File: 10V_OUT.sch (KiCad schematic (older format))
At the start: 25 parts, among them U8 LM324

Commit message: Finished the schematic, except for maybe a couple test points.
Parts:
- removed U8: LM324, Package_DIP:DIP-14_W7.62mm, symbol Amplifier_Operational:LM324
- added U10: TLV9304IDR, Package_SO:SOIC-14_3.9x8.7mm_P1.27mm, symbol Amplifier_Operational:TLV9004xRUCR
- renumbered C27 to C36, C28 to C37, C29 to C38, C30 to C39, C31 to C40, C32 to C41, C33 to C42, C34 to C43, R62 to R65, R63 to R66, R64 to R67, R65 to R68, R66 to R69, R67 to R70, R68 to R71, R69 to R72, R70 to R73, R71 to R74, R72 to R75, R73 to R76, R74 to R77, R75 to R78, R76 to R79, R77 to R80

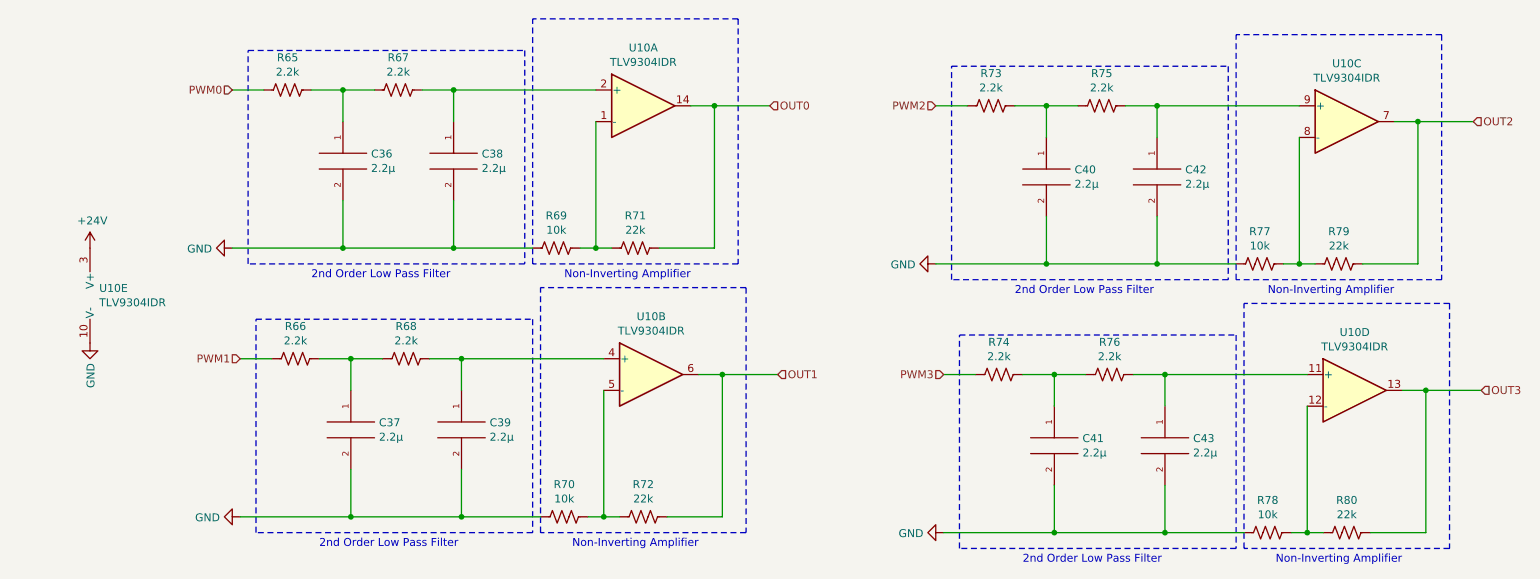
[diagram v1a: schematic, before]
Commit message: Routing for all analog outputs
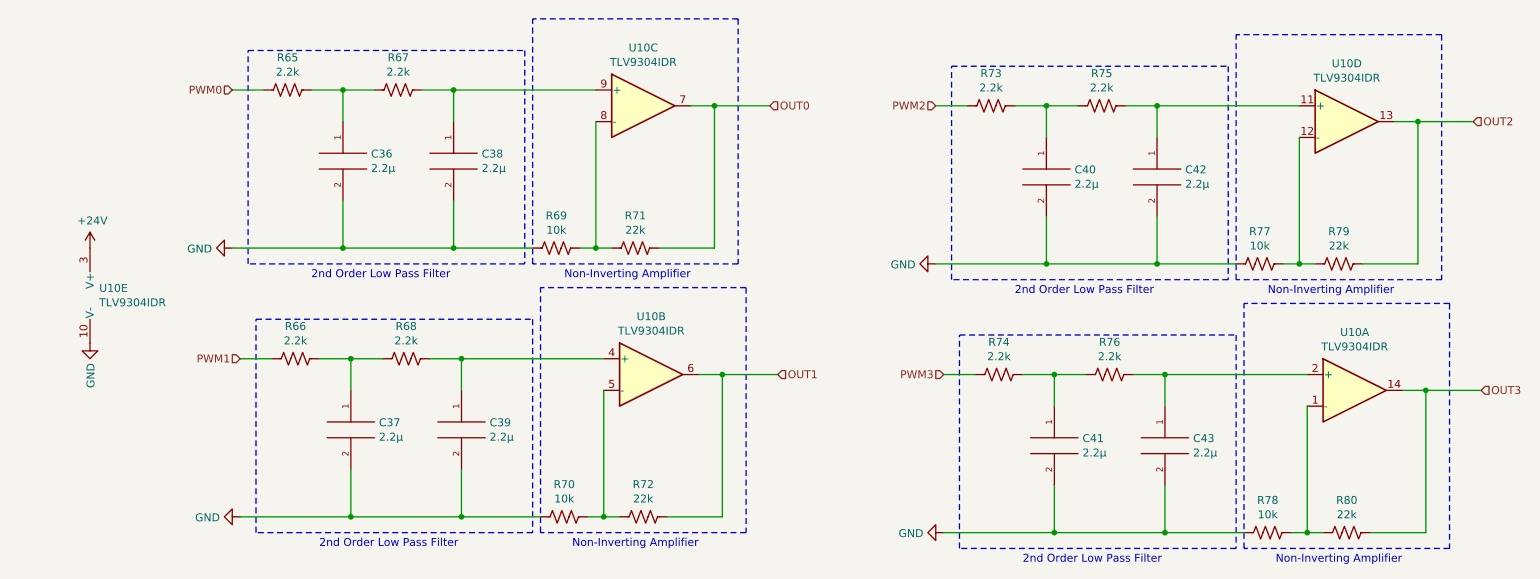
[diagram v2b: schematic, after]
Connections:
- net OUT0: now also U10.7; no longer U10.14
- net OUT2: now also U10.13; no longer U10.7
- net OUT3: now also U10.14; no longer U10.13
- net at C38.1, R67.1: now also U10.9 (+); no longer U10.2 (+)
- net at R69.1, R71.2: now also U10.8 (-); no longer U10.1 (-)
- net at C42.1, R75.1: now also U10.11 (+); no longer U10.9 (+)
- net at R77.1, R79.2: now also U10.12 (-); no longer U10.8 (-)
- net at C43.1, R76.1: now also U10.2 (+); no longer U10.11 (+)
- net at R78.1, R80.2: now also U10.1 (-); no longer U10.12 (-)
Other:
- moved on the sheet: U10A, U10C, U10D
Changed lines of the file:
@@
 L Amplifier_Operational:TLV9004xRUCR U10
 U 1 1 61E28A21
-P 4850 2200
-F 0 "U10" H 4850 2567 50  0000 C CNN
-F 1 "TLV9304IDR" H 4850 2476 50  0000 C CNN
-F 2 "Package_SO:SOIC-14_3.9x8.7mm_P1.27mm" H 4850 2200 50  0001 C CNN
-F 3 "http://www.ti.com/lit/ds/symlink/tlv9004.pdf" H 4900 2400 50  0001 C CNN
-	1    4850 2200
+P 9350 4000
+F 0 "U10" H 9350 4367 50  0000 C CNN
+F 1 "TLV9304IDR" H 9350 4276 50  0000 C CNN
+F 2 "Package_SO:SOIC-14_3.9x8.7mm_P1.27mm" H 9350 4000 50  0001 C CNN
+F 3 "http://www.ti.com/lit/ds/symlink/tlv9004.pdf" H 9400 4200 50  0001 C CNN
+	1    9350 4000
 	1    0    0    -1
 $EndComp
@@
 L Amplifier_Operational:TLV9004xRUCR U10
 U 3 1 61E31CB3
+P 4850 2200
+F 0 "U10" H 4850 2567 50  0000 C CNN
+F 1 "TLV9304IDR" H 4850 2476 50  0000 C CNN
+F 2 "Package_SO:SOIC-14_3.9x8.7mm_P1.27mm" H 4850 2200 50  0001 C CNN
+F 3 "http://www.ti.com/lit/ds/symlink/tlv9004.pdf" H 4900 2400 50  0001 C CNN
+	3    4850 2200
+	1    0    0    -1
+$EndComp
+$Comp
+L Amplifier_Operational:TLV9004xRUCR U10
+U 4 1 61E32B03
 P 9300 2300
 F 0 "U10" H 9300 2667 50  0000 C CNN
@@
 F 2 "Package_SO:SOIC-14_3.9x8.7mm_P1.27mm" H 9300 2300 50  0001 C CNN
 F 3 "http://www.ti.com/lit/ds/symlink/tlv9004.pdf" H 9350 2500 50  0001 C CNN
-	3    9300 2300
+	4    9300 2300
 	1    0    0    -1
 $EndComp
-$Comp
-L Amplifier_Operational:TLV9004xRUCR U10
-U 4 1 61E32B03
-P 9350 4000
-F 0 "U10" H 9350 4367 50  0000 C CNN
-F 1 "TLV9304IDR" H 9350 4276 50  0000 C CNN
-F 2 "Package_SO:SOIC-14_3.9x8.7mm_P1.27mm" H 9350 4000 50  0001 C CNN
-F 3 "http://www.ti.com/lit/ds/symlink/tlv9004.pdf" H 9400 4200 50  0001 C CNN
-	4    9350 4000
-	1    0    0    -1
-$EndComp
